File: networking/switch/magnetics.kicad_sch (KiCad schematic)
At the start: 0 parts

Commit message: Feat[switch]: added sheet metadata and magnetics symbols to sch
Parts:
- added T1, T2: Quad Transformer, symbol magnetics:quad-transformer
- added U2: Single Transformer, symbol magnetics:single-transformer
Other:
- company: (none) -> MUREX Robotics [Byran Huang and Max Liu]
- title: (none) -> MUREX Ethernet Switch (needs a better name)
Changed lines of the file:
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@@
 (kicad_sch (version 20230409) (generator eeschema)
   (paper "A4")
+  (title_block
+    (title "MUREX Ethernet Switch (needs a better name)")
+    (date "2023-08-30")
+    (rev "V1.0")
+    (company "MUREX Robotics [Byran Huang and Max Liu]")
+    (comment 3 "// INNOVATION FOR ALL.")
+    (comment 4 "// ATTEMPT THE IMPOSSIBLE.")
+  )
+  (symbol (lib_id "magnetics:quad-transformer") (at 133.35 138.43 0) (unit 1)
+    (in_bom yes) (on_board yes) (dnp no) (fields_autoplaced)
+    (property "Reference" "T2" (at 133.35 116.84 0)
+      (effects (font (size 1.27 1.27)))
+    )
+    (property "Value" "Quad Transformer" (at 133.35 119.38 0)
+      (effects (font (size 1.27 1.27)))
+    )
+    (property "Footprint" "" (at 133.35 137.16 0)
+      (effects (font (size 1.27 1.27)) hide)
+    )
+    (property "Datasheet" "" (at 133.35 137.16 0)
+      (effects (font (size 1.27 1.27)) hide)
+    )
+    (pin "1")
+    (pin "10")
+    (pin "11")
+    (pin "12")
+    (pin "13")
+    (pin "14")
+    (pin "15")
+    (pin "16")
+    (pin "17")
+    (pin "18")
+    (pin "19")
+    (pin "2")
+    (pin "20")
+    (pin "3")
+    (pin "4")
+    (pin "5")
+    (pin "6")
+    (pin "7")
+    (pin "8")
+    (pin "9")
+    (instances
+      (project "switch"
+        (path "/3a8c8799-9295-4740-b990-f123ec1feb18/3b4e3a24-52bc-4456-b8ba-0ef7b116b867"
+          (reference "T2") (unit 1)
+        )
+      )
+    )
+  )
+  (symbol (lib_id "magnetics:single-transformer") (at 133.35 57.15 0) (unit 1)
+    (in_bom yes) (on_board yes) (dnp no) (fields_autoplaced)
+    (property "Reference" "U2" (at 133.35 40.64 0)
+      (effects (font (size 1.27 1.27)))
+    )
+    (property "Value" "Single Transformer" (at 133.35 43.18 0)
+      (effects (font (size 1.27 1.27)))
+    )
+    (property "Footprint" "" (at 133.35 57.15 0)
+      (effects (font (size 1.27 1.27)) hide)
+    )
+    (property "Datasheet" "" (at 133.35 57.15 0)
+      (effects (font (size 1.27 1.27)) hide)
+    )
+    (pin "1")
+    (pin "10")
+    (pin "11")
+    (pin "12")
+    (pin "13")
+    (pin "14")
+    (pin "15")
+    (pin "16")
+    (pin "2")
+    (pin "3")
+    (pin "4")
+    (pin "5")
+    (pin "6")
+    (pin "7")
+    (pin "8")
+    (pin "9")
+    (instances
+      (project "switch"
+        (path "/3a8c8799-9295-4740-b990-f123ec1feb18/3b4e3a24-52bc-4456-b8ba-0ef7b116b867"
+          (reference "U2") (unit 1)
+        )
+      )
+    )
+  )
+  (symbol (lib_id "magnetics:quad-transformer") (at 133.35 95.25 0) (unit 1)
+    (in_bom yes) (on_board yes) (dnp no) (fields_autoplaced)
+    (property "Reference" "T1" (at 133.35 73.66 0)
+      (effects (font (size 1.27 1.27)))
+    )
+    (property "Value" "Quad Transformer" (at 133.35 76.2 0)
+      (effects (font (size 1.27 1.27)))
+    )
+    (property "Footprint" "" (at 133.35 93.98 0)
+      (effects (font (size 1.27 1.27)) hide)
+    )
+    (property "Datasheet" "" (at 133.35 93.98 0)
+      (effects (font (size 1.27 1.27)) hide)
+    )
+    (pin "1")
+    (pin "10")
+    (pin "11")
+    (pin "12")
+    (pin "13")
+    (pin "14")
+    (pin "15")
+    (pin "16")
+    (pin "17")
+    (pin "18")
+    (pin "19")
+    (pin "2")
+    (pin "20")
+    (pin "3")
+    (pin "4")
+    (pin "5")
+    (pin "6")
+    (pin "7")
+    (pin "8")
+    (pin "9")
+    (instances
+      (project "switch"
+        (path "/3a8c8799-9295-4740-b990-f123ec1feb18/3b4e3a24-52bc-4456-b8ba-0ef7b116b867"
+          (reference "T1") (unit 1)
+        )
+      )
+    )
+  )
 )

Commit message: Feat[switch]: further work on schematic
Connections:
- net RXIP1: now reaches T2.1 (RD2+)
- net RXIP0: now reaches T2.10 (RD1+)
- net RX0+: now reaches T2.11 (RX1+)
- net RX0+: now also T2.14 (TX1+)
- net RX0-: now reaches T2.12 (RX1-)
- net REF0: now reaches T2.13 (CMG1)
- net TX0-: now reaches T2.15 (TX1-)
- net TX1-: now reaches T2.16 (TX2-)
- net TX1+: now reaches T2.17 (TX2+)
- net REF1: now reaches T2.18 (CMG0)
- net RX1-: now reaches T2.19 (RX2-)
- net RMIM1: now reaches T2.2 (RD2-)
- net RX1+: now reaches T2.20 (RX2+)
- net TXOP1: now reaches T2.4 (TD2+)
- net TXOM1: now reaches T2.5 (TD2-)
- net TXOM0: now reaches T2.6 (TD1-)
- net TXOP0: now reaches T2.7 (TD1+)
- net RXIM0: now reaches T2.9 (RD1-)
- net RXIP4: now reaches U2.1 (TD+)
- net TX4+: now reaches U2.11 (RX+)
- net RX4-: now reaches U2.14 (TX-)
- net RX4+: now reaches U2.16 (TX+)
- net RXIM4: now reaches U2.3 (TD-)
- net TXOP4: now reaches U2.6 (RT+)
- net TXOM4: now reaches U2.8 (RX-)
- net TX4-: now reaches U2.9 (RX-)
- net TXOM3: now reaches T1.1 (RD2+)
- net RXIP2: now reaches T1.10 (RD1+)
- net RX2+: now reaches T1.11 (RX1+)
- net RX2-: now reaches T1.12 (RX1-)
- net REF2: now reaches T1.13 (CMG1)
- net TX2+: now reaches T1.14 (TX1+)
- net TX2-: now reaches T1.15 (TX1-)
- net RX3+: now reaches T1.16 (TX2-)
- net RX3-: now reaches T1.17 (TX2+)
- net REF3: now reaches T1.18 (CMG0)
- net TX3+: now reaches T1.19 (RX2-)
- net TXOP3: now reaches T1.2 (RD2-)
- net TX3-: now reaches T1.20 (RX2+)
- net CT3: now reaches T1.3 (CT2)
- net RXIM3: now reaches T1.4 (TD2+)
- net RXIP3: now reaches T1.5 (TD2-)
- net TXOM2: now reaches T1.6 (TD1-)
- net TXOP2: now reaches T1.7 (TD1+)
- net CT2: now reaches T1.8 (CT1)
- net RXIM2: now reaches T1.9 (RD1-)
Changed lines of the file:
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@@
     (rev "V1.0")
     (company "MUREX Robotics [Byran Huang and Max Liu]")
-    (comment 3 "// INNOVATION FOR ALL.")
+    (comment 1 "utilizing the IC Plus IP175G and external magnetics")
+    (comment 2 "Ultra-compact 5 port unmanaged ethernet switch")
+    (comment 3 "// TECHNOLOGY FOR ALL.")
     (comment 4 "// ATTEMPT THE IMPOSSIBLE.")
   )
+  (hierarchical_label "REF2" (shape bidirectional) (at 147.32 99.06 0) (fields_autoplaced)
+    (effects (font (size 1.27 1.27)) (justify left))
+  )
+  (hierarchical_label "RX2-" (shape bidirectional) (at 147.32 107.95 0) (fields_autoplaced)
+    (effects (font (size 1.27 1.27)) (justify left))
+  )
+  (hierarchical_label "TXOP1" (shape bidirectional) (at 119.38 130.81 180) (fields_autoplaced)
+    (effects (font (size 1.27 1.27)) (justify right))
+  )
+  (hierarchical_label "CT3" (shape bidirectional) (at 119.38 92.71 180) (fields_autoplaced)
+    (effects (font (size 1.27 1.27)) (justify right))
+  )
+  (hierarchical_label "RXIP2" (shape bidirectional) (at 119.38 110.49 180) (fields_autoplaced)
+    (effects (font (size 1.27 1.27)) (justify right))
+  )
+  (hierarchical_label "TX2+" (shape bidirectional) (at 147.32 104.14 0) (fields_autoplaced)
+    (effects (font (size 1.27 1.27)) (justify left))
+  )
+  (hierarchical_label "TXOM2" (shape bidirectional) (at 119.38 99.06 180) (fields_autoplaced)
+    (effects (font (size 1.27 1.27)) (justify right))
+  )
+  (hierarchical_label "RMIM1" (shape bidirectional) (at 119.38 125.73 180) (fields_autoplaced)
+    (effects (font (size 1.27 1.27)) (justify right))
+  )
+  (hierarchical_label "TX1-" (shape bidirectional) (at 147.32 135.89 0) (fields_autoplaced)
+    (effects (font (size 1.27 1.27)) (justify left))
+  )
+  (hierarchical_label "RXIM3" (shape bidirectional) (at 119.38 87.63 180) (fields_autoplaced)
+    (effects (font (size 1.27 1.27)) (justify right))
+  )
+  (hierarchical_label "TXOP3" (shape bidirectional) (at 119.38 82.55 180) (fields_autoplaced)
+    (effects (font (size 1.27 1.27)) (justify right))
+  )
+  (hierarchical_label "TXOM3" (shape bidirectional) (at 119.38 80.01 180) (fields_autoplaced)
+    (effects (font (size 1.27 1.27)) (justify right))
+  )
+  (hierarchical_label "RX0+" (shape bidirectional) (at 147.32 153.67 0) (fields_autoplaced)
+    (effects (font (size 1.27 1.27)) (justify left))
+  )
+  (hierarchical_label "RXIP3" (shape bidirectional) (at 119.38 90.17 180) (fields_autoplaced)
+    (effects (font (size 1.27 1.27)) (justify right))
+  )
+  (hierarchical_label "REF3" (shape bidirectional) (at 147.32 87.63 0) (fields_autoplaced)
+    (effects (font (size 1.27 1.27)) (justify left))
+  )
+  (hierarchical_label "TXOM0" (shape bidirectional) (at 119.38 142.24 180) (fields_autoplaced)
+    (effects (font (size 1.27 1.27)) (justify right))
+  )
+  (hierarchical_label "TX4+" (shape bidirectional) (at 147.32 60.96 0) (fields_autoplaced)
+    (effects (font (size 1.27 1.27)) (justify left))
+  )
+  (hierarchical_label "RX4+" (shape bidirectional) (at 147.32 48.26 0) (fields_autoplaced)
+    (effects (font (size 1.27 1.27)) (justify left))
+  )
+  (hierarchical_label "TXOP0" (shape bidirectional) (at 119.38 144.78 180) (fields_autoplaced)
+    (effects (font (size 1.27 1.27)) (justify right))
+  )
+  (hierarchical_label "REF1" (shape bidirectional) (at 147.32 130.81 0) (fields_autoplaced)
+    (effects (font (size 1.27 1.27)) (justify left))
+  )
+  (hierarchical_label "RXIM0" (shape bidirectional) (at 119.38 151.13 180) (fields_autoplaced)
+    (effects (font (size 1.27 1.27)) (justify right))
+  )
+  (hierarchical_label "RX3-" (shape bidirectional) (at 147.32 90.17 0) (fields_autoplaced)
+    (effects (font (size 1.27 1.27)) (justify left))
+  )
+  (hierarchical_label "CT2" (shape bidirectional) (at 119.38 104.14 180) (fields_autoplaced)
+    (effects (font (size 1.27 1.27)) (justify right))
+  )
+  (hierarchical_label "REF0" (shape bidirectional) (at 147.32 142.24 0) (fields_autoplaced)
+    (effects (font (size 1.27 1.27)) (justify left))
+  )
+  (hierarchical_label "TX2-" (shape bidirectional) (at 147.32 101.6 0) (fields_autoplaced)
+    (effects (font (size 1.27 1.27)) (justify left))
+  )
+  (hierarchical_label "RX0+" (shape bidirectional) (at 147.32 147.32 0) (fields_autoplaced)
+    (effects (font (size 1.27 1.27)) (justify left))
+  )
+  (hierarchical_label "RX2+" (shape bidirectional) (at 147.32 110.49 0) (fields_autoplaced)
+    (effects (font (size 1.27 1.27)) (justify left))
+  )
+  (hierarchical_label "RXIP0" (shape bidirectional) (at 119.38 153.67 180) (fields_autoplaced)
+    (effects (font (size 1.27 1.27)) (justify right))
+  )
+  (hierarchical_label "RX1+" (shape bidirectional) (at 147.32 123.19 0) (fields_autoplaced)
+    (effects (font (size 1.27 1.27)) (justify left))
+  )
+  (hierarchical_label "TX1+" (shape bidirectional) (at 147.32 133.35 0) (fields_autoplaced)
+    (effects (font (size 1.27 1.27)) (justify left))
+  )
+  (hierarchical_label "RX0-" (shape bidirectional) (at 147.32 151.13 0) (fields_autoplaced)
+    (effects (font (size 1.27 1.27)) (justify left))
+  )
+  (hierarchical_label "TXOP4" (shape bidirectional) (at 119.38 60.96 180) (fields_autoplaced)
+    (effects (font (size 1.27 1.27)) (justify right))
+  )
+  (hierarchical_label "RX4-" (shape bidirectional) (at 147.32 53.34 0) (fields_autoplaced)
+    (effects (font (size 1.27 1.27)) (justify left))
+  )
+  (hierarchical_label "TXOM1" (shape bidirectional) (at 119.38 133.35 180) (fields_autoplaced)
+    (effects (font (size 1.27 1.27)) (justify right))
+  )
+  (hierarchical_label "RXIM2" (shape bidirectional) (at 119.38 107.95 180) (fields_autoplaced)
+    (effects (font (size 1.27 1.27)) (justify right))
+  )
+  (hierarchical_label "RXIP1" (shape bidirectional) (at 119.38 123.19 180) (fields_autoplaced)
+    (effects (font (size 1.27 1.27)) (justify right))
+  )
+  (hierarchical_label "RXIP4" (shape bidirectional) (at 119.38 48.26 180) (fields_autoplaced)
+    (effects (font (size 1.27 1.27)) (justify right))
+  )
+  (hierarchical_label "RX3+" (shape bidirectional) (at 147.32 92.71 0) (fields_autoplaced)
+    (effects (font (size 1.27 1.27)) (justify left))
+  )
+  (hierarchical_label "TX3-" (shape bidirectional) (at 147.32 80.01 0) (fields_autoplaced)
+    (effects (font (size 1.27 1.27)) (justify left))
+  )
+  (hierarchical_label "TX4-" (shape bidirectional) (at 147.32 66.04 0) (fields_autoplaced)
+    (effects (font (size 1.27 1.27)) (justify left))
+  )
+  (hierarchical_label "TXOP2" (shape bidirectional) (at 119.38 101.6 180) (fields_autoplaced)
+    (effects (font (size 1.27 1.27)) (justify right))
+  )
+  (hierarchical_label "TX0-" (shape bidirectional) (at 147.32 144.78 0) (fields_autoplaced)
+    (effects (font (size 1.27 1.27)) (justify left))
+  )
+  (hierarchical_label "TX3+" (shape bidirectional) (at 147.32 82.55 0) (fields_autoplaced)
+    (effects (font (size 1.27 1.27)) (justify left))
+  )
+  (hierarchical_label "RX1-" (shape bidirectional) (at 147.32 125.73 0) (fields_autoplaced)
+    (effects (font (size 1.27 1.27)) (justify left))
+  )
+  (hierarchical_label "RXIM4" (shape bidirectional) (at 119.38 53.34 180) (fields_autoplaced)
+    (effects (font (size 1.27 1.27)) (justify right))
+  )
+  (hierarchical_label "TXOM4" (shape bidirectional) (at 119.38 66.04 180) (fields_autoplaced)
+    (effects (font (size 1.27 1.27)) (justify right))
+  )
   (symbol (lib_id "magnetics:quad-transformer") (at 133.35 138.43 0) (unit 1)

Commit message: Fix[switch]: renamed quad to dual transformer
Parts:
- removed T1, T2: Quad Transformer, symbol magnetics:quad-transformer
- added T1, T2: Dual Transformer, symbol magnetics:dual-transformer
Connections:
- net CT2: now also T1.8 (CT1)
- net CT3: now also T1.3 (CT2)
- net REF0: now also T2.13 (CMG1)
- net REF1: now also T2.18 (CMG0)
- net REF2: now also T1.13 (CMG1)
- net REF3: now also T1.18 (CMG0)
- net RMIM1: now also T2.2 (RD2-)
- net RX0+: now also T2.11 (RX1+), T2.14 (TX1+)
- net RX0-: now also T2.12 (RX1-)
- net RX1+: now also T2.20 (RX2+)
- net RX1-: now also T2.19 (RX2-)
- net RX2+: now also T1.11 (RX1+)
- net RX2-: now also T1.12 (RX1-)
- net RX3+: now also T1.16 (TX2-)
- net RX3-: now also T1.17 (TX2+)
- net RXIM0: now also T2.9 (RD1-)
- net RXIM2: now also T1.9 (RD1-)
- net RXIM3: now also T1.4 (TD2+)
- net RXIP0: now also T2.10 (RD1+)
- net RXIP1: now also T2.1 (RD2+)
- net RXIP2: now also T1.10 (RD1+)
- net RXIP3: now also T1.5 (TD2-)
- net TX0-: now also T2.15 (TX1-)
- net TX1+: now also T2.17 (TX2+)
- net TX1-: now also T2.16 (TX2-)
- net TX2+: now also T1.14 (TX1+)
- net TX2-: now also T1.15 (TX1-)
- net TX3+: now also T1.19 (RX2-)
- net TX3-: now also T1.20 (RX2+)
- net TXOM0: now also T2.6 (TD1-)
- net TXOM1: now also T2.5 (TD2-)
- net TXOM2: now also T1.6 (TD1-)
- net TXOM3: now also T1.1 (RD2+)
- net TXOP0: now also T2.7 (TD1+)
- net TXOP1: now also T2.4 (TD2+)
- net TXOP2: now also T1.7 (TD1+)
- net TXOP3: now also T1.2 (RD2-)
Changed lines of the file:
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@@
     (effects (font (size 1.27 1.27)) (justify right))
   )
-  (symbol (lib_id "magnetics:quad-transformer") (at 133.35 138.43 0) (unit 1)
+  (symbol (lib_id "magnetics:dual-transformer") (at 133.35 138.43 0) (unit 1)
     (in_bom yes) (on_board yes) (dnp no) (fields_autoplaced)
     (property "Reference" "T2" (at 133.35 116.84 0)
       (effects (font (size 1.27 1.27)))
     )
-    (property "Value" "Quad Transformer" (at 133.35 119.38 0)
+    (property "Value" "Dual Transformer" (at 133.35 119.38 0)
       (effects (font (size 1.27 1.27)))
     )
@@
     )
   )
-  (symbol (lib_id "magnetics:quad-transformer") (at 133.35 95.25 0) (unit 1)
+  (symbol (lib_id "magnetics:dual-transformer") (at 133.35 95.25 0) (unit 1)
     (in_bom yes) (on_board yes) (dnp no) (fields_autoplaced)
     (property "Reference" "T1" (at 133.35 73.66 0)
       (effects (font (size 1.27 1.27)))
     )
-    (property "Value" "Quad Transformer" (at 133.35 76.2 0)
+    (property "Value" "Dual Transformer" (at 133.35 76.2 0)
       (effects (font (size 1.27 1.27)))
     )

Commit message: Feat[switch]: unpolished schematic complete
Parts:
- added C27, C29, C30, C31, C32: 0.1uF, symbol Device:C_Small
- added C28, C33: 1nF 2KV (1206), symbol Device:C_Small
- added J2: PHY 5, symbol Connector_Generic:Conn_01x04
- added J3: PHY 4, symbol Connector_Generic:Conn_01x04
- added J4: PHY 3, symbol Connector_Generic:Conn_01x04
- added J5: PHY 2, symbol Connector_Generic:Conn_01x04
- added J6: PHY 1, symbol Connector_Generic:Conn_01x04
- added R14, R17, R18, R19, R20: 75, symbol Device:R_Small
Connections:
- net CT2: now also C30.1
- net CT3: now also C29.1
- net REF0: now also C33.1, R17.2, R18.2, R19.2, R20.2; no longer T2.13 (CMG1)
- net RX0+: now also J6.3 (Pin_3)
- net RX0-: now also J6.4 (Pin_4)
- net RX1+: now also J5.3 (Pin_3)
- net RX1-: now also J5.4 (Pin_4)
- net RX2+: now also J4.3 (Pin_3)
- net RX2-: now also J4.4 (Pin_4)
- net RX3+: now also J3.3 (Pin_3)
- net RX3-: now also J3.4 (Pin_4)
- net RX4+: now also J2.3 (Pin_3)
- net RX4-: now also J2.4 (Pin_4)
- net TX0-: now also J6.2 (Pin_2)
- net TX1+: now also J5.1 (Pin_1)
- net TX1-: now also J5.2 (Pin_2)
- net TX2+: now also J4.1 (Pin_1)
- net TX2-: now also J4.2 (Pin_2)
- net TX3+: now also J3.1 (Pin_1)
- net TX3-: now also J3.2 (Pin_2)
- net TX4+: now also J2.1 (Pin_1)
- net TX4-: now also J2.2 (Pin_2)
- net CT1: now reaches T2.3 (CT2)
- net CT1: now also C31.1
- net CT0: now reaches T2.8 (CT1)
- net CT0: now also C32.1
- net REF4: now reaches U2.10 (MCT)
- net REF4: now also U2.13 (MCT), U2.15 (MCT), R14.1
- net CT4: now reaches U2.2 (CT)
- net CT4: now also U2.5 (CT), U2.7 (CT), C27.1
- net REF1: no longer names the net of T2.18 (CMG0)
- net REF1: now also R17.1
- net REF2: no longer names the net of T1.13 (CMG1)
- net REF2: now also R19.1
- net REF3: no longer names the net of T1.18 (CMG0)
- net REF3: now also R20.1
- net RMIM1 renamed RXIM1
- new net: C28.1, R14.2
- new net: R18.1, T2.13 (CMG1)
- new net Earth: C28.2, C33.2
- new net GND: C27.2, C29.2, C30.2, C31.2, C32.2
- new net TX0+: J6.1 (Pin_1)
- no-connect marks 0 -> 2
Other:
- note added: "Pinout: TX+, TX-, RX+, RX-"
- note added: "most likely molex picoblades"

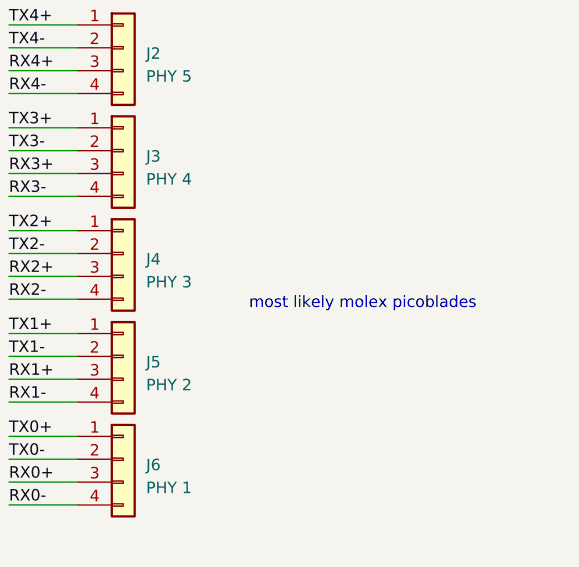
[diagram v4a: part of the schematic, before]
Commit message: Refactor[switch]: net labels and reorganisation
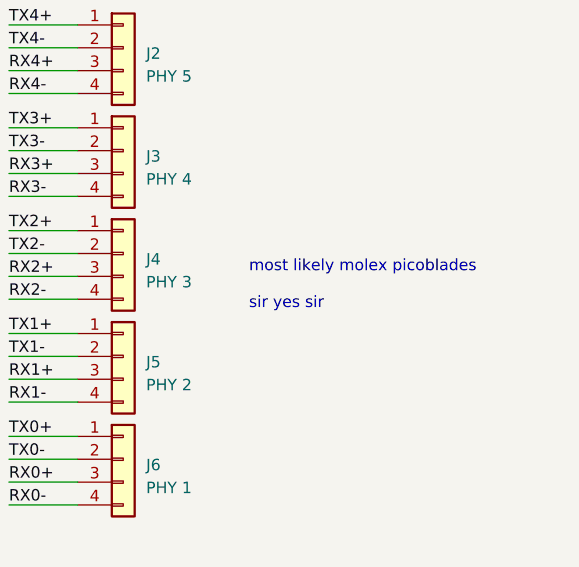
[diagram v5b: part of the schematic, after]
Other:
- note added: "most likely molex picoblades sir yes sir"
- note removed: "most likely molex picoblades"
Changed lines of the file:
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@@
     (effects (font (size 1.27 1.27)) (justify left bottom))
   )
-  (text "most likely molex picoblades" (exclude_from_sim no)
+  (text "most likely molex picoblades\n\nsir yes sir" (exclude_from_sim no)
  (at 232.41 91.44 0)
     (effects (font (size 1.27 1.27)) (justify left bottom))

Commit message: Feat[switch]: refactored schematic complete
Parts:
- renumbered C27 to C24, C29 to C25, C31 to C26, C30 to C27, C32 to C28, C28 to C29, C33 to C30, J2 to J3, J3 to J4, J4 to J5, J5 to J6, J6 to J7, R20 to R21, R19 to R22, R17 to R23, R18 to R24, R14 to R25, U2 to U4
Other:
- note added: "1x4 picoblades"
- note removed: "most likely molex picoblades sir yes sir"
- title: MUREX Ethernet Switch (needs a better name) -> MUREX Ethernet Switch
